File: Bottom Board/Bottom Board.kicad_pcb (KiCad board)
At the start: 2 copper layers, 88.9 x 27.9 mm, 5 parts

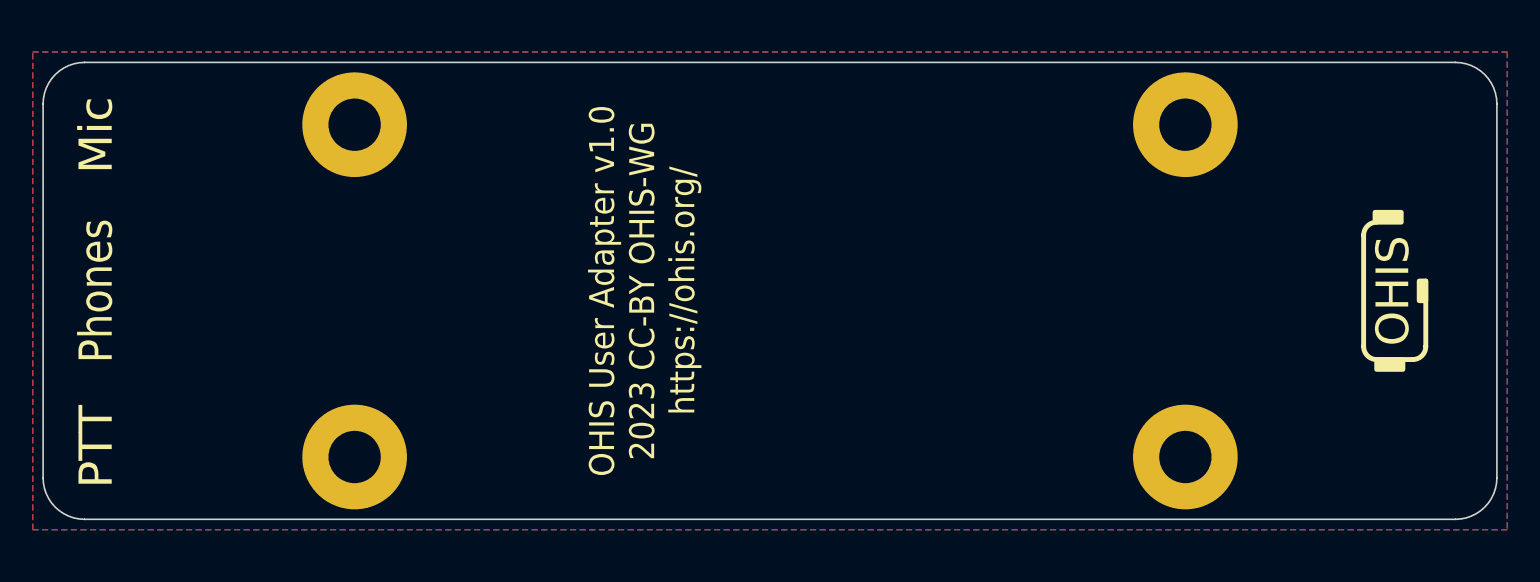
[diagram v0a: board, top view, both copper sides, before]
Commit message: Fixed silkscreen art, added trimpot. #1
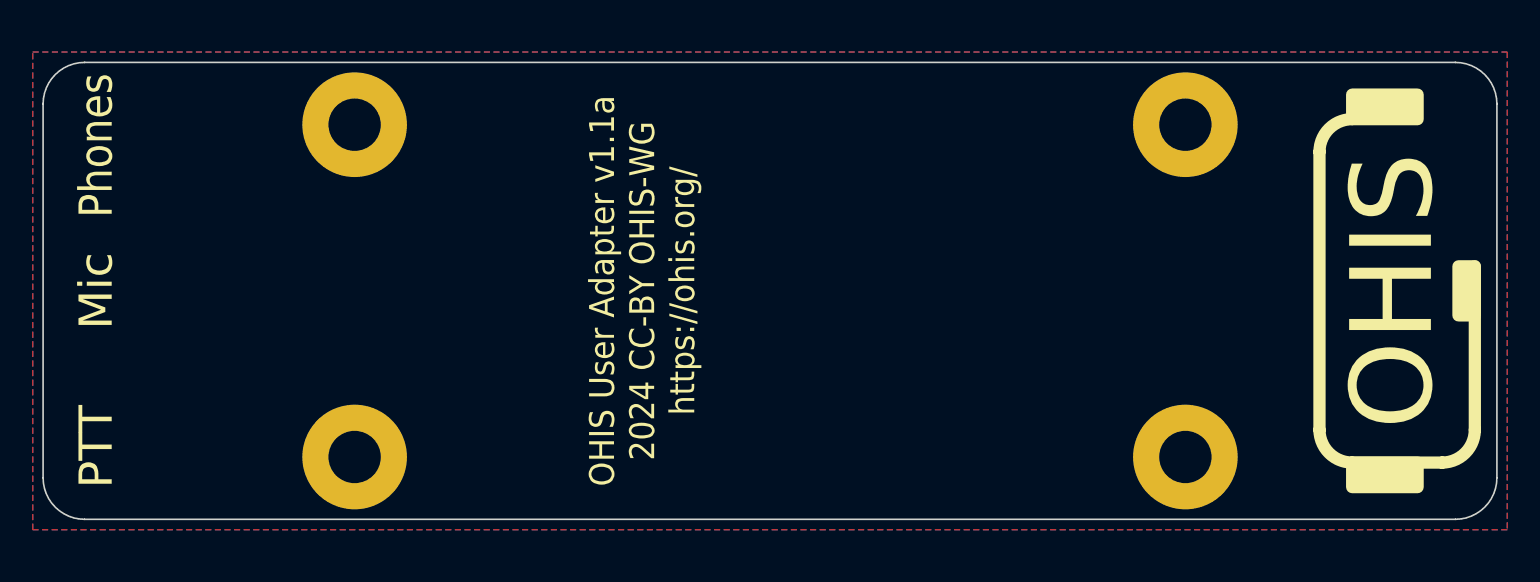
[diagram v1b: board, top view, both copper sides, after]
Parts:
- added G2: Logo_OHIS, Libraries:Logo_OHIS_Medium, B.Cu at (146.1, 76.2)
- G1: footprint Libraries:Logo_OHIS_Medium -> Libraries:Logo_OHIS_Large
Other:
- board text added: "JLCJLCJLCJLC"
- board text added: "OHIS User Adapter v1.1a 2024 CC-BY OHIS-WG https://ohis.org/"
- board text removed: "OHIS User Adapter v1.0 2023 CC-BY OHIS-WG https://ohis.org/"
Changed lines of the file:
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@@
     (descr "Mounting Hole 3.2mm, M3")
     (tags "mounting hole 3.2mm m3")
-    (property "Sheetfile" "Top Board.kicad_sch")
+    (property "Sheetfile" "Bottom Board.kicad_sch")
     (property "Sheetname" "")
     (property "ki_description" "Mounting Hole with connection")
@@
       (net 1 "GND") (pinfunction "1") (pintype "input"))
   )
-  (footprint "Libraries:Logo_OHIS_Medium" (layer "F.Cu")
+  (footprint "Libraries:Logo_OHIS_Large" (layer "F.Cu")
     (at 146.05 76.2 90)
-    (property "Sheetfile" "Top Board.kicad_sch")
+    (property "Sheetfile" "Bottom Board.kicad_sch")
     (property "Sheetname" "")
     (property "exclude_from_bom" "")
@@
     )
     (fp_text user "OHIS" (at 0 0 90 unlocked) (layer "F.SilkS")
-        (effects (font (size 2 2) (thickness 0.3)))
+        (effects (font (size 5 5) (thickness 0.75)))
     )
     (fp_text user "${REFERENCE}" (at 0 2.5 90 unlocked) (layer "F.Fab") hide
         (effects (font (size 1 1) (thickness 0.15)))
     )
-    (fp_line (start -4.200001 1.2) (end -4.2 -1)
-      (stroke (width 0.3) (type solid)) (layer "F.SilkS"))
-    (fp_line (start 0.6 2) (end -3.400001 2)
-      (stroke (width 0.3) (type solid)) (layer "F.SilkS"))
-    (fp_line (start 3.4 -1.8) (end -3.4 -1.8)
-      (stroke (width 0.3) (type solid)) (layer "F.SilkS"))
-    (fp_rect (start -4.2 0.6) (end -4.8 -1)
-      (stroke (width 0.3) (type solid)) (fill solid) (layer "F.SilkS"))
-    (fp_rect (start 0.6 2) (end -0.6 1.6)
-      (stroke (width 0.3) (type solid)) (fill solid) (layer "F.SilkS"))
-    (fp_rect (start 4.8 0.5) (end 4.2 -1.1)
-      (stroke (width 0.3) (type solid)) (fill solid) (layer "F.SilkS"))
-    (fp_arc (start -4.2 -1) (mid -3.965685 -1.565685) (end -3.4 -1.8)
-      (stroke (width 0.3) (type solid)) (layer "F.SilkS"))
-    (fp_arc (start -3.400001 2) (mid -3.965686 1.765685) (end -4.200001 1.2)
-      (stroke (width 0.3) (type solid)) (layer "F.SilkS"))
-    (fp_arc (start 3.4 -1.8) (mid 3.965685 -1.565685) (end 4.2 -1)
-      (stroke (width 0.3) (type solid)) (layer "F.SilkS"))
+    (fp_line (start -10.5 -2.5) (end -10.5 2.999999)
+      (stroke (width 0.75) (type solid)) (layer "F.SilkS"))
+    (fp_line (start 1.5 5) (end -8.499999 4.999999)
+      (stroke (width 0.75) (type solid)) (layer "F.SilkS"))
+    (fp_line (start 8.499999 -4.499999) (end -8.5 -4.5)
+      (stroke (width 0.75) (type solid)) (layer "F.SilkS"))
+    (fp_rect (start -10.5 -2.5) (end -12 1.5)
+      (stroke (width 0.75) (type solid)) (fill solid) (layer "F.SilkS"))
+    (fp_rect (start 1.5 4) (end -1.5 5)
+      (stroke (width 0.75) (type solid)) (fill solid) (layer "F.SilkS"))
+    (fp_rect (start 11.999999 -2.499999) (end 10.499999 1.500001)
+      (stroke (width 0.75) (type solid)) (fill solid) (layer "F.SilkS"))
+    (fp_arc (start -10.5 -2.5) (mid -9.914214 -3.914214) (end -8.5 -4.5)
+      (stroke (width 0.75) (type solid)) (layer "F.SilkS"))
+    (fp_arc (start -8.499999 4.999999) (mid -9.914213 4.414213) (end -10.499999 2.999999)
+      (stroke (width 0.75) (type solid)) (layer "F.SilkS"))
+    (fp_arc (start 8.499999 -4.499999) (mid 9.914213 -3.914213) (end 10.499999 -2.499999)
+      (stroke (width 0.75) (type solid)) (layer "F.SilkS"))
   )
   (footprint "MountingHole:MountingHole_3.2mm_M3_Pad" locked (layer "F.Cu")
@@
     (descr "Mounting Hole 3.2mm, M3")
     (tags "mounting hole 3.2mm m3")
-    (property "Sheetfile" "Top Board.kicad_sch")
+    (property "Sheetfile" "Bottom Board.kicad_sch")
     (property "Sheetname" "")
     (property "ki_description" "Mounting Hole with connection")
@@
     (descr "Mounting Hole 3.2mm, M3")
     (tags "mounting hole 3.2mm m3")
-    (property "Sheetfile" "Top Board.kicad_sch")
+    (property "Sheetfile" "Bottom Board.kicad_sch")
     (property "Sheetname" "")
     (property "ki_description" "Mounting Hole with connection")
@@
     (descr "Mounting Hole 3.2mm, M3")
     (tags "mounting hole 3.2mm m3")
-    (property "Sheetfile" "Top Board.kicad_sch")
+    (property "Sheetfile" "Bottom Board.kicad_sch")
     (property "Sheetname" "")
     (property "ki_description" "Mounting Hole with connection")
@@
     (pad "1" thru_hole circle locked (at 0 0) (size 6.4 6.4) (drill 3.2) (layers "*.Cu" "*.Mask")
       (net 1 "GND") (pinfunction "1") (pintype "input"))
+  )
+  (footprint "Libraries:Logo_OHIS_Medium" (layer "B.Cu")
+    (at 146.05 76.2 -90)
+    (property "Sheetfile" "Bottom Board.kicad_sch")
+    (property "Sheetname" "")
+    (property "exclude_from_bom" "")
+    (attr exclude_from_bom)
+    (fp_text reference "G2" (at 0 0.5 90 unlocked) (layer "B.SilkS") hide
+        (effects (font (size 1 1) (thickness 0.15)) (justify mirror))
+    )
+    (fp_text value "Logo_OHIS" (at 0 -1 90 unlocked) (layer "B.Fab") hide
+        (effects (font (size 1 1) (thickness 0.15)) (justify mirror))
+    )
+    (fp_text user "OHIS" (at 0 0 90 unlocked) (layer "B.SilkS")
+        (effects (font (size 2 2) (thickness 0.3)) (justify mirror))
+    )
+    (fp_text user "${REFERENCE}" (at 0 -2.5 90 unlocked) (layer "B.Fab") hide
+        (effects (font (size 1 1) (thickness 0.15)) (justify mirror))
+    )
+    (fp_line (start -4.200001 -1.2) (end -4.2 1)
+      (stroke (width 0.3) (type solid)) (layer "B.SilkS"))
+    (fp_line (start 0.6 -2) (end -3.400001 -2)
+      (stroke (width 0.3) (type solid)) (layer "B.SilkS"))
+    (fp_line (start 3.4 1.8) (end -3.4 1.8)
+      (stroke (width 0.3) (type solid)) (layer "B.SilkS"))
+    (fp_rect (start -4.2 -0.6) (end -4.8 1)
+      (stroke (width 0.3) (type solid)) (fill solid) (layer "B.SilkS"))
+    (fp_rect (start 0.6 -2) (end -0.6 -1.6)
+      (stroke (width 0.3) (type solid)) (fill solid) (layer "B.SilkS"))
+    (fp_rect (start 4.8 -0.5) (end 4.2 1.1)
+      (stroke (width 0.3) (type solid)) (fill solid) (layer "B.SilkS"))
+    (fp_arc (start -4.200001 -1.2) (mid -3.965686 -1.765685) (end -3.400001 -2)
+      (stroke (width 0.3) (type solid)) (layer "B.SilkS"))
+    (fp_arc (start -3.4 1.8) (mid -3.965685 1.565685) (end -4.2 1)
+      (stroke (width 0.3) (type solid)) (layer "B.SilkS"))
+    (fp_arc (start 4.2 1) (mid 3.965685 1.565685) (end 3.4 1.8)
+      (stroke (width 0.3) (type solid)) (layer "B.SilkS"))
   )
   (gr_line (start 158.115 76.2) (end 57.15 76.2)
@@
   (gr_arc locked (start 149.86 62.23) (mid 151.656051 62.973949) (end 152.4 64.77)
     (stroke (width 0.1) (type default)) (layer "Edge.Cuts"))
-  (gr_text "Mic" (at 67.945 66.675 90) (layer "F.SilkS")
+  (gr_text "Mic" (at 67.945 76.2 90) (layer "B.SilkS")
+    (effects (font (size 2.032 2.032) (thickness 0.254)) (justify bottom mirror))
+  )
+  (gr_text "JLCJLCJLCJLC" (at 107.95 76.2) (layer "B.SilkS")
+    (effects (font (size 1.524 1.397) (thickness 0.2032)) (justify mirror))
+  )
+  (gr_text "Phones" (at 67.945 85.09 90) (layer "B.SilkS")
+    (effects (font (size 2.032 1.778) (thickness 0.254)) (justify bottom mirror))
+  )
+  (gr_text "PTT" (at 67.945 66.675 90) (layer "B.SilkS")
+    (effects (font (size 2.032 2.032) (thickness 0.254)) (justify bottom mirror))
+  )
+  (gr_text "Mic" (at 67.945 76.2 90) (layer "F.SilkS")
     (effects (font (size 2.032 2.032) (thickness 0.254)) (justify bottom))
   )
-  (gr_text "OHIS User Adapter v1.0\n2023 CC-BY OHIS-WG\nhttps://ohis.org/" (at 103.505 76.2 90) (layer "F.SilkS")
+  (gr_text "OHIS User Adapter v1.1a\n2024 CC-BY OHIS-WG\nhttps://ohis.org/" (at 103.505 76.2 90) (layer "F.SilkS")
     (effects (font (size 1.524 1.397) (thickness 0.2032)) (justify bottom))
   )
-  (gr_text "Phones" (at 67.945 76.2 90) (layer "F.SilkS")
+  (gr_text "Phones" (at 67.945 67.31 90) (layer "F.SilkS")
     (effects (font (size 2.032 1.778) (thickness 0.254)) (justify bottom))
   )

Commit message: Cleaned up board, moved jumpers to right-angle at board edge.
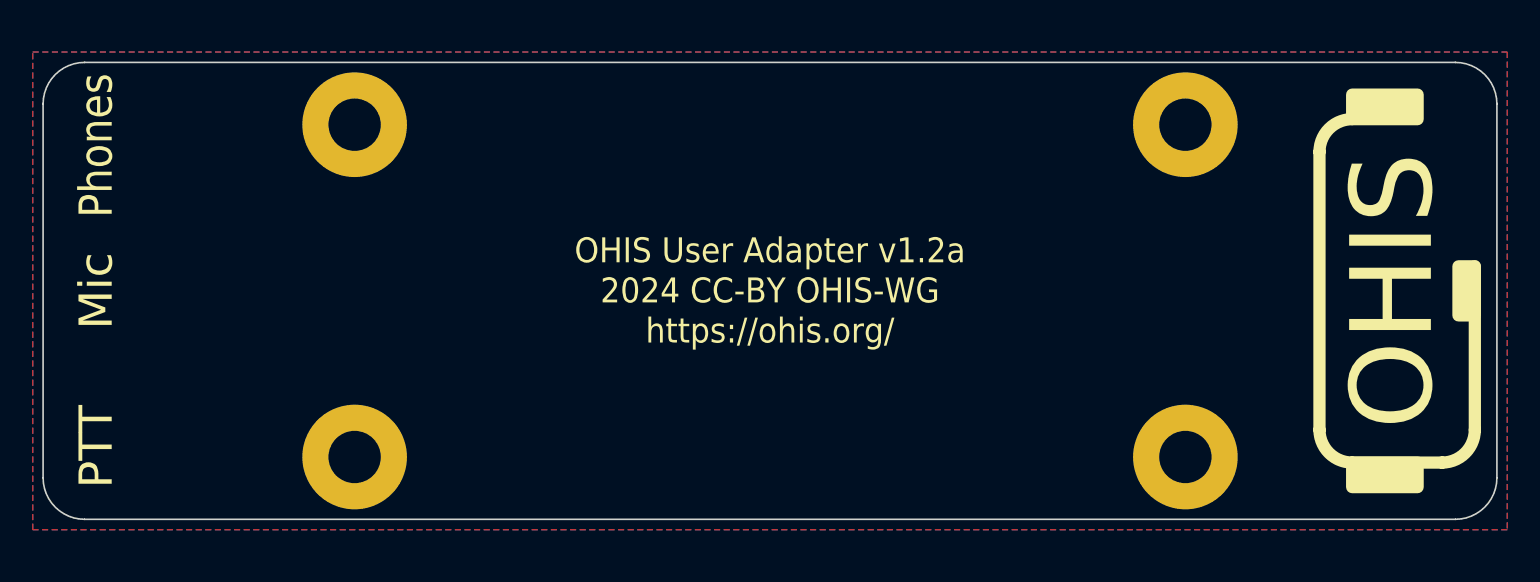
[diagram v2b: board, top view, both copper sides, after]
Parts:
- removed G2: Logo_OHIS, Libraries:Logo_OHIS_Medium
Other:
- board text added: "OHIS User Adapter v1.2a 2024 CC-BY OHIS-WG https://ohis.org/"
- board text removed: "OHIS User Adapter v1.1a 2024 CC-BY OHIS-WG https://ohis.org/"
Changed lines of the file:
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@@
       (net 1 "GND") (pinfunction "1") (pintype "input"))
-  )
-  (footprint "Libraries:Logo_OHIS_Medium" (layer "B.Cu")
-    (at 146.05 76.2 -90)
-    (property "Sheetfile" "Bottom Board.kicad_sch")
-    (property "Sheetname" "")
-    (property "exclude_from_bom" "")
-    (attr exclude_from_bom)
-    (fp_text reference "G2" (at 0 0.5 90 unlocked) (layer "B.SilkS") hide
-        (effects (font (size 1 1) (thickness 0.15)) (justify mirror))
-    )
-    (fp_text value "Logo_OHIS" (at 0 -1 90 unlocked) (layer "B.Fab") hide
-        (effects (font (size 1 1) (thickness 0.15)) (justify mirror))
-    )
-    (fp_text user "OHIS" (at 0 0 90 unlocked) (layer "B.SilkS")
-        (effects (font (size 2 2) (thickness 0.3)) (justify mirror))
-    )
-    (fp_text user "${REFERENCE}" (at 0 -2.5 90 unlocked) (layer "B.Fab") hide
-        (effects (font (size 1 1) (thickness 0.15)) (justify mirror))
-    )
-    (fp_line (start -4.200001 -1.2) (end -4.2 1)
-      (stroke (width 0.3) (type solid)) (layer "B.SilkS"))
-    (fp_line (start 0.6 -2) (end -3.400001 -2)
-      (stroke (width 0.3) (type solid)) (layer "B.SilkS"))
-    (fp_line (start 3.4 1.8) (end -3.4 1.8)
-      (stroke (width 0.3) (type solid)) (layer "B.SilkS"))
-    (fp_rect (start -4.2 -0.6) (end -4.8 1)
-      (stroke (width 0.3) (type solid)) (fill solid) (layer "B.SilkS"))
-    (fp_rect (start 0.6 -2) (end -0.6 -1.6)
-      (stroke (width 0.3) (type solid)) (fill solid) (layer "B.SilkS"))
-    (fp_rect (start 4.8 -0.5) (end 4.2 1.1)
-      (stroke (width 0.3) (type solid)) (fill solid) (layer "B.SilkS"))
-    (fp_arc (start -4.200001 -1.2) (mid -3.965686 -1.765685) (end -3.400001 -2)
-      (stroke (width 0.3) (type solid)) (layer "B.SilkS"))
-    (fp_arc (start -3.4 1.8) (mid -3.965685 1.565685) (end -4.2 1)
-      (stroke (width 0.3) (type solid)) (layer "B.SilkS"))
-    (fp_arc (start 4.2 1) (mid 3.965685 1.565685) (end 3.4 1.8)
-      (stroke (width 0.3) (type solid)) (layer "B.SilkS"))
   )
   (gr_line (start 158.115 76.2) (end 57.15 76.2)
@@
   (gr_arc locked (start 149.86 62.23) (mid 151.656051 62.973949) (end 152.4 64.77)
     (stroke (width 0.1) (type default)) (layer "Edge.Cuts"))
-  (gr_text "Mic" (at 67.945 76.2 90) (layer "B.SilkS")
-    (effects (font (size 2.032 2.032) (thickness 0.254)) (justify bottom mirror))
-  )
   (gr_text "JLCJLCJLCJLC" (at 107.95 76.2) (layer "B.SilkS")
     (effects (font (size 1.524 1.397) (thickness 0.2032)) (justify mirror))
-  )
-  (gr_text "Phones" (at 67.945 85.09 90) (layer "B.SilkS")
-    (effects (font (size 2.032 1.778) (thickness 0.254)) (justify bottom mirror))
-  )
-  (gr_text "PTT" (at 67.945 66.675 90) (layer "B.SilkS")
-    (effects (font (size 2.032 2.032) (thickness 0.254)) (justify bottom mirror))
   )
   (gr_text "Mic" (at 67.945 76.2 90) (layer "F.SilkS")
     (effects (font (size 2.032 2.032) (thickness 0.254)) (justify bottom))
   )
-  (gr_text "OHIS User Adapter v1.1a\n2024 CC-BY OHIS-WG\nhttps://ohis.org/" (at 103.505 76.2 90) (layer "F.SilkS")
-    (effects (font (size 1.524 1.397) (thickness 0.2032)) (justify bottom))
+  (gr_text "OHIS User Adapter v1.2a\n2024 CC-BY OHIS-WG\nhttps://ohis.org/" (at 107.95 76.2) (layer "F.SilkS")
+    (effects (font (size 1.524 1.397) (thickness 0.2032)))
   )
   (gr_text "Phones" (at 67.945 67.31 90) (layer "F.SilkS")
@@
     (pts (xy 83.185 76.2) (xy 63.5 76.2))
     (height 17.78)
-    (gr_text "0.7750 in" (at 73.3425 57.27) (layer "Dwgs.User")
+    (gr_text "19.6850 mm" (at 73.3425 57.27) (layer "Dwgs.User")
       (effects (font (size 1 1) (thickness 0.15)))
     )
@@
     (pts (xy 63.5 76.2) (xy 63.5 85.725))
     (height 2.54)
-    (gr_text "0.3750 in" (at 59.81 80.9625 90) (layer "Dwgs.User")
+    (gr_text "9.5250 mm" (at 59.81 80.9625 90) (layer "Dwgs.User")
       (effects (font (size 1 1) (thickness 0.15)))
     )
@@
     (pts (xy 63.5 76.2) (xy 63.5 66.675))
     (height -2.54)
-    (gr_text "0.3750 in" (at 59.81 71.4375 90) (layer "Dwgs.User")
+    (gr_text "9.5250 mm" (at 59.81 71.4375 90) (layer "Dwgs.User")
       (effects (font (size 1 1) (thickness 0.15)))
     )

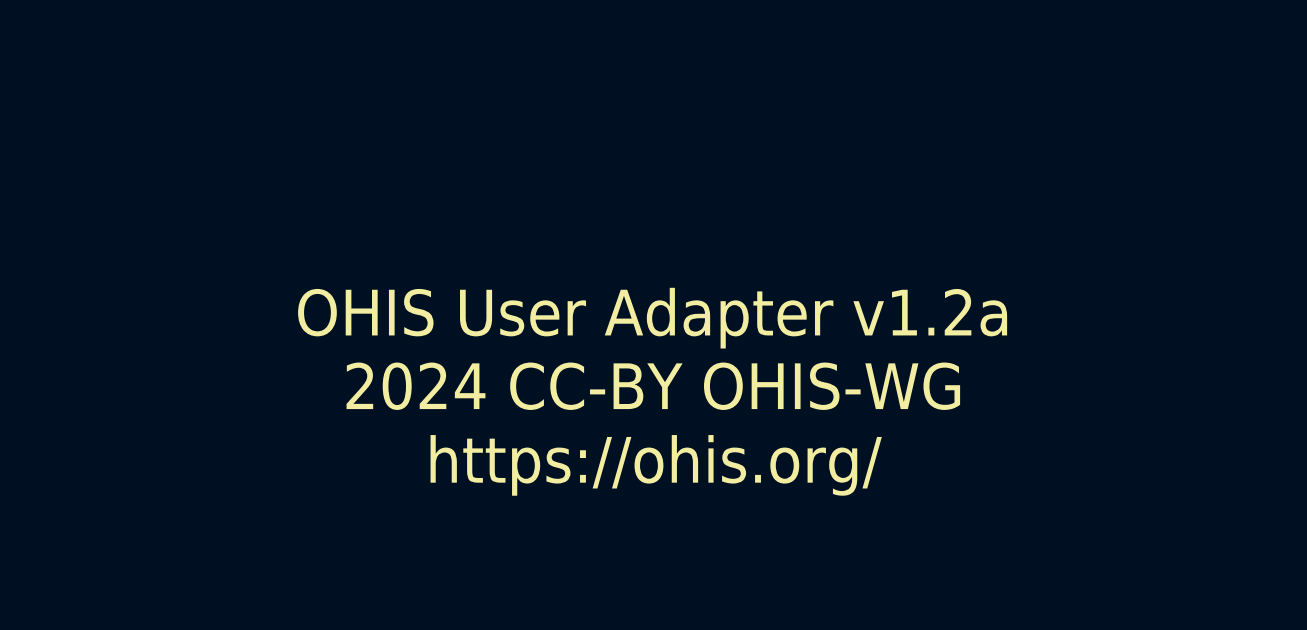
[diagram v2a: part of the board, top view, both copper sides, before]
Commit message: update top and bottom board silk screen to v1.3a
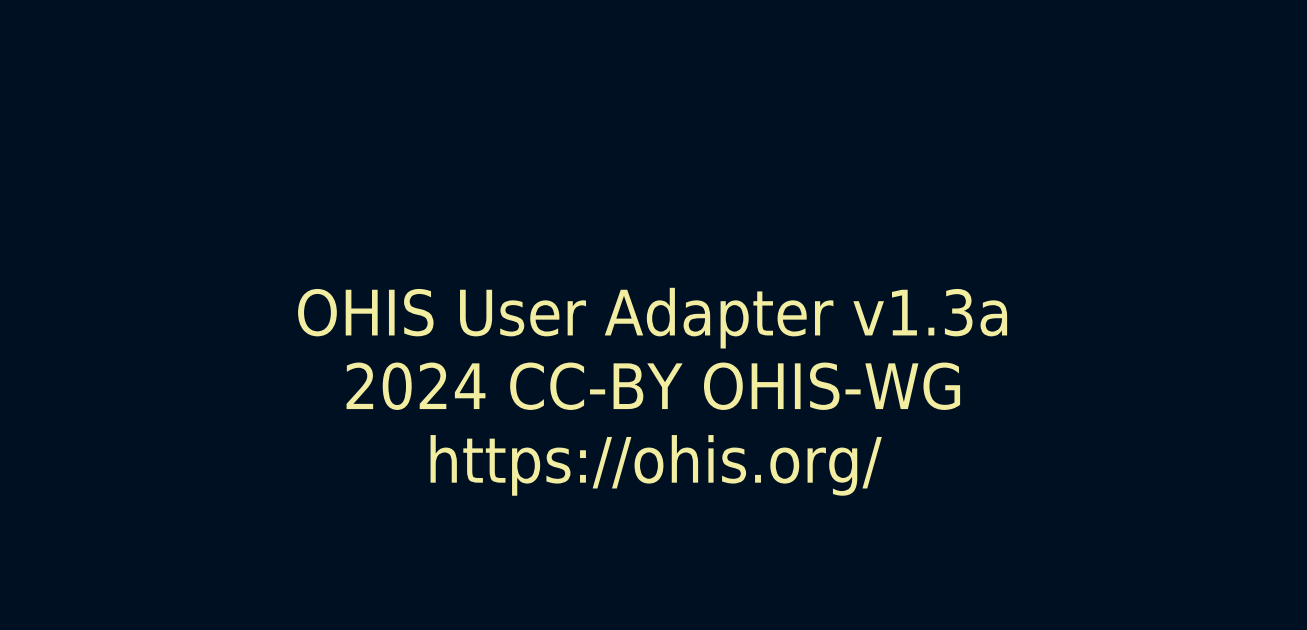
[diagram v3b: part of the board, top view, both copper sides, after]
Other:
- board text added: "OHIS User Adapter v1.3a 2024 CC-BY OHIS-WG https://ohis.org/"
- board text removed: "OHIS User Adapter v1.2a 2024 CC-BY OHIS-WG https://ohis.org/"
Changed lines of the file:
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@@
       (outputformat 1)
       (mirror false)
-      (drillshape 1)
+      (drillshape 0)
       (scaleselection 1)
-      (outputdirectory "")
+      (outputdirectory "C:/Users/derek.HOME/Desktop/user_adapter_v1.3a/bottom_board")
     )
   )
@@
     (effects (font (size 2.032 2.032) (thickness 0.254)) (justify bottom))
   )
-  (gr_text "OHIS User Adapter v1.2a\n2024 CC-BY OHIS-WG\nhttps://ohis.org/" (at 107.95 76.2) (layer "F.SilkS")
+  (gr_text "OHIS User Adapter v1.3a\n2024 CC-BY OHIS-WG\nhttps://ohis.org/" (at 107.95 76.2) (layer "F.SilkS")
     (effects (font (size 1.524 1.397) (thickness 0.2032)))
   )
